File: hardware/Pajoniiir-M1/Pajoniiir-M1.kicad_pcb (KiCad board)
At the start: 4 copper layers, 0 parts

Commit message: feat: establish board-first B8 pre-layout
Populate the live PCB with the complete schematic footprint/net set, preserve fail-closed mechanical gates, and isolate DSI506 as a qualified display profile. Add reproducible placement validation, ERC/BOM evidence, and synchronized project documentation.
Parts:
- added C1: 100nF, Capacitor_SMD:C_0603_1608Metric, F.Cu at (41.9, 93.6)
- added C101: 100nF, Capacitor_SMD:C_0603_1608Metric, F.Cu at (43.6, 232.4)
- added C102: 1uF, Capacitor_SMD:C_0603_1608Metric, F.Cu at (60.6, 232.4)
- added C103: 470pF >=25V, Capacitor_SMD:C_0402_1005Metric, F.Cu at (54.1, 208.7)
- added C104: 100nF, Capacitor_SMD:C_0603_1608Metric, F.Cu at (49.6, 232.4)
- added C105: 10uF, Capacitor_SMD:C_0805_2012Metric, F.Cu at (55.3, 232.7)
- added C106: 22uF DNP, Capacitor_SMD:C_1206_3216Metric, F.Cu at (24.9, 232.8)
- added C107: DNP SI TUNE, Capacitor_SMD:C_0402_1005Metric, F.Cu at (34.9, 232.1)
- added C108: DNP EMI TUNE, Capacitor_SMD:C_0402_1005Metric, F.Cu at (111.3, 241.7)
- added C109: DNP EMI TUNE, Capacitor_SMD:C_0402_1005Metric, F.Cu at (123.6, 241.7)
- added C110: 100nF, Capacitor_SMD:C_0603_1608Metric, F.Cu at (48.0, 93.6)
- added C111: 100nF, Capacitor_SMD:C_0603_1608Metric, F.Cu at (54.1, 93.6)
- added C112: 1uF, Capacitor_SMD:C_0603_1608Metric, F.Cu at (68.3, 101.1)
- added C2: 10uF, Capacitor_SMD:C_0805_2012Metric, F.Cu at (57.9, 101.4)
- added C20: 10uF >=10V, Capacitor_SMD:C_0805_2012Metric, F.Cu at (59.1, 72.6)
- added C21: 100nF >=10V, Capacitor_SMD:C_0603_1608Metric, F.Cu at (70.7, 72.3)
- added C22: 3.3nF, Capacitor_SMD:C_0603_1608Metric, F.Cu at (41.4, 101.1)
- added C23: 22uF >=6.3V, Capacitor_SMD:C_1206_3216Metric, F.Cu at (69.1, 66.1)
- added C24: 22uF DNP RESERVE, Capacitor_SMD:C_1206_3216Metric, F.Cu at (45.5, 53.8)
- added C25: 100nF, Capacitor_SMD:C_0603_1608Metric, F.Cu at (60.1, 93.6)
- added C26: 100nF, Capacitor_SMD:C_0603_1608Metric, F.Cu at (69.3, 158.9)
- added C27: 10nF, Capacitor_SMD:C_0402_1005Metric, F.Cu at (83.5, 170.7)
- added C28: 100nF, Capacitor_SMD:C_0603_1608Metric, F.Cu at (75.3, 158.9)
- added C29: 4.7uF, Capacitor_SMD:C_0603_1608Metric, F.Cu at (47.5, 170.9)
- added C30: 1uF, Capacitor_SMD:C_0603_1608Metric, F.Cu at (22.6, 177.2)
- added C31: 100nF, Capacitor_SMD:C_0603_1608Metric, F.Cu at (81.4, 158.9)
- added C32: 1uF, Capacitor_SMD:C_0603_1608Metric, F.Cu at (26.9, 177.2)
- added C33: 100nF, Capacitor_SMD:C_0603_1608Metric, F.Cu at (87.5, 158.9)
- added C34: 1uF, Capacitor_SMD:C_0603_1608Metric, F.Cu at (31.3, 177.2)
- added C35: 100nF, Capacitor_SMD:C_0603_1608Metric, F.Cu at (23.4, 165.2)
- added C36: 1uF, Capacitor_SMD:C_0603_1608Metric, F.Cu at (35.6, 177.2)
- added C37: 1uF, Capacitor_SMD:C_0603_1608Metric, F.Cu at (40.0, 177.2)
- added C38: 10nF, Capacitor_SMD:C_0402_1005Metric, F.Cu at (88.6, 170.7)
- added C39: 100nF, Capacitor_SMD:C_0603_1608Metric, F.Cu at (29.5, 165.2)
- added C4: 4.7nF, Capacitor_SMD:C_0603_1608Metric, F.Cu at (47.0, 101.1)
- added C40: 4.7uF, Capacitor_SMD:C_0805_2012Metric, F.Cu at (63.4, 159.2)
- added C41: 22uF, Capacitor_SMD:C_0805_2012Metric, F.Cu at (52.8, 171.2)
- added C42: 22pF C0G, Capacitor_SMD:C_0402_1005Metric, F.Cu at (72.4, 149.7)
- added C43: 10uF, Capacitor_SMD:C_0805_2012Metric, F.Cu at (57.9, 171.2)
- added C44: 100nF, Capacitor_SMD:C_0603_1608Metric, F.Cu at (35.6, 165.2)
- added C45: 100nF, Capacitor_SMD:C_0603_1608Metric, F.Cu at (41.6, 165.2)
- added C46: 100nF, Capacitor_SMD:C_0603_1608Metric, F.Cu at (47.7, 165.2)
- added C47: 100nF, Capacitor_SMD:C_0603_1608Metric, F.Cu at (53.8, 165.2)
- added C48: 10uF, Capacitor_SMD:C_0805_2012Metric, F.Cu at (63.1, 171.2)
- added C49: 100nF, Capacitor_SMD:C_0603_1608Metric, F.Cu at (59.8, 165.2)
- added C5: 4.7nF, Capacitor_SMD:C_0603_1608Metric, F.Cu at (52.6, 101.1)
- added C50: 100nF, Capacitor_SMD:C_0603_1608Metric, F.Cu at (65.9, 165.2)
- added C51: 100nF, Capacitor_SMD:C_0603_1608Metric, F.Cu at (72.0, 165.2)
- added C52: 100nF, Capacitor_SMD:C_0603_1608Metric, F.Cu at (78.1, 165.2)
- added C53: 100nF, Capacitor_SMD:C_0603_1608Metric, F.Cu at (84.1, 165.2)
- added C54: 100nF, Capacitor_SMD:C_0603_1608Metric, F.Cu at (23.4, 170.9)
- added C55: 10uF, Capacitor_SMD:C_0805_2012Metric, F.Cu at (68.2, 171.2)
- added C56: 100nF, Capacitor_SMD:C_0603_1608Metric, F.Cu at (29.5, 170.9)
- added C57: 10uF, Capacitor_SMD:C_0805_2012Metric, F.Cu at (73.3, 171.2)
- added C58: 100nF, Capacitor_SMD:C_0603_1608Metric, F.Cu at (35.6, 170.9)
- added C59: 10uF, Capacitor_SMD:C_0805_2012Metric, F.Cu at (78.4, 171.2)
- added C6: 100nF, Capacitor_SMD:C_0603_1608Metric, F.Cu at (66.2, 93.6)
- added C60: 100nF, Capacitor_SMD:C_0603_1608Metric, F.Cu at (41.6, 170.9)
- added C61: 15pF C0G, Capacitor_SMD:C_0402_1005Metric, F.Cu at (81.2, 149.7)
- added C62: 15pF C0G, Capacitor_SMD:C_0402_1005Metric, F.Cu at (24.8, 158.6)
- added C63: 1uF, Capacitor_SMD:C_0603_1608Metric, F.Cu at (44.4, 177.2)
- added C64: 100nF, Capacitor_SMD:C_0603_1608Metric, F.Cu at (138.6, 165.9)
- added C65: 10uF, Capacitor_SMD:C_0805_2012Metric, F.Cu at (144.2, 166.1)
- added C66: 22uF, Capacitor_SMD:C_1206_3216Metric, F.Cu at (132.7, 166.3)
- added C67: 1uF, Capacitor_SMD:C_0603_1608Metric, F.Cu at (106.6, 172.5)
- added C68: 10uF, Capacitor_SMD:C_0805_2012Metric, F.Cu at (63.1, 101.4)
- added C69: 100nF, Capacitor_SMD:C_0603_1608Metric, F.Cu at (72.3, 93.6)
- added C7: 22uF, Capacitor_SMD:C_1206_3216Metric, F.Cu at (36.0, 94.0)
- added C70: 100nF, Capacitor_SMD:C_0603_1608Metric, F.Cu at (23.4, 101.1)
- added C71: 47uF, Capacitor_SMD:C_1210_3225Metric, F.Cu at (70.4, 87.0)
- added C72: 100uF DNP, Capacitor_SMD:C_1210_3225Metric, F.Cu at (38.7, 73.2)
- added C73: 100nF, Capacitor_SMD:C_0603_1608Metric, F.Cu at (29.5, 101.1)
- added C74: 100nF, Capacitor_SMD:C_0603_1608Metric, F.Cu at (35.6, 101.1)
- added C75: 47uF, Capacitor_SMD:C_1210_3225Metric, F.Cu at (23.3, 94.5)
- added C76: 100uF DNP, Capacitor_SMD:C_1210_3225Metric, F.Cu at (48.6, 73.2)
- added C77: 1nF DNP, Capacitor_SMD:C_0603_1608Metric, F.Cu at (119.0, 69.5)
- added C78: DNP EMI TUNE, Capacitor_SMD:C_0402_1005Metric, F.Cu at (96.6, 69.2)
- added C79: DNP EMI TUNE, Capacitor_SMD:C_0402_1005Metric, F.Cu at (108.9, 69.2)
- added C80: 1nF DNP, Capacitor_SMD:C_0603_1608Metric, F.Cu at (127.0, 69.5)
- added C81: 10uF, Capacitor_SMD:C_0805_2012Metric, F.Cu at (179.4, 60.3)
- added C82: 100nF, Capacitor_SMD:C_0603_1608Metric, F.Cu at (191.0, 44.2)
- added C83: 10uF, Capacitor_SMD:C_0805_2012Metric, F.Cu at (184.5, 60.3)
- added C84: 100nF, Capacitor_SMD:C_0603_1608Metric, F.Cu at (150.4, 60.1)
- added C85: 10uF, Capacitor_SMD:C_0805_2012Metric, F.Cu at (189.6, 60.3)
- added C86: 100nF, Capacitor_SMD:C_0603_1608Metric, F.Cu at (156.5, 60.1)
- added C87: 10uF, Capacitor_SMD:C_0805_2012Metric, F.Cu at (150.0, 66.6)
- added C88: 2.2uF, Capacitor_SMD:C_0603_1608Metric, F.Cu at (168.4, 60.1)
- added C89: 2.2uF, Capacitor_SMD:C_0603_1608Metric, F.Cu at (174.0, 60.1)
- added C90: 100nF, Capacitor_SMD:C_0603_1608Metric, F.Cu at (162.6, 60.1)
- added C91: 2.2nF C0G, Capacitor_SMD:C_0603_1608Metric, F.Cu at (174.0, 44.2)
- added C92: 2.2nF C0G, Capacitor_SMD:C_0603_1608Metric, F.Cu at (183.3, 44.2)
- added C93: 100nF, Capacitor_SMD:C_0603_1608Metric, F.Cu at (179.4, 147.6)
- added C94: 10uF, Capacitor_SMD:C_0805_2012Metric, F.Cu at (185.0, 147.9)
- added D1: SMBJ6.0CA-TR, Diode_SMD:D_SMB, F.Cu at (53.8, 45.9)
- added D2: TPD2EUSB30ADRTR, Package_TO_SOT_SMD:Texas_DRT-3, F.Cu at (115.5, 28.3)
- added D3: TPD2EUSB30ADRTR, Package_TO_SOT_SMD:Texas_DRT-3, F.Cu at (115.5, 48.9)
- added FB1: 0R / FERRITE OPTION, Resistor_SMD:R_0603_1608Metric, F.Cu at (29.4, 60.0)
- added FB2: 0R / FERRITE OPTION, Resistor_SMD:R_0603_1608Metric, F.Cu at (47.4, 60.0)
- added FB3: 0R / ferrite option, Resistor_SMD:R_0603_1608Metric, F.Cu at (168.4, 147.6)
- added J10: C6 DEBUG TC2030-NL DNL, Connector:Tag-Connect_TC2030-IDC-NL_2x03_P1.27mm_Vertical, F.Cu at (91.5, 228.6)
- added J2: 87520-1010ALF, Pajoniiir-M1:Amphenol_87520-1010ALF, F.Cu at (95.6, 30.0)
- added J3: 87520-1010ALF, Pajoniiir-M1:Amphenol_87520-1010ALF, F.Cu at (95.6, 50.6)
- added J4: KLPX-0848A-2-W-G, Pajoniiir-M1:Kycon_KLPX-0848A-2-x-G, F.Cu at (174.5, 33.3)
- added J5: KLPX-0848A-2-R-G, Pajoniiir-M1:Kycon_KLPX-0848A-2-x-G, F.Cu at (162.1, 49.2)
- added J6: 15-pin Raspberry-Pi-style DSI host, Pajoniiir-M1:Amphenol_SFW15R-2STE1LF, F.Cu at (175.2, 137.5)
- added J7: 503398-1892, Pajoniiir-M1:Molex_503398-1892, F.Cu at (27.8, 217.8)
- added J8: P4 DEBUG TC2030-NL DNL, Connector:Tag-Connect_TC2030-IDC-NL_2x03_P1.27mm_Vertical, F.Cu at (91.5, 209.8)
- added J9: P4 USB SERIAL/JTAG FACTORY POGO DNL, Pajoniiir-M1:Factory_Pogo_USBJTAG_1x05_P1.27_2Tooling, F.Cu at (96.9, 219.4)
- added L1: XGL4030-222MEC / 2.2uH, Inductor_SMD:L_Coilcraft_XxL4030, F.Cu at (31.4, 151.6)
- added L2: XGL4030-222MEC / 2.2uH, Inductor_SMD:L_Coilcraft_XxL4030, F.Cu at (59.0, 29.8)
- added R1: 402k 1%, Resistor_SMD:R_0603_1608Metric, F.Cu at (32.6, 86.1)
- added R100: 4.7k DNP, Resistor_SMD:R_0603_1608Metric, F.Cu at (174.5, 160.2)
- added R104: 100k, Resistor_SMD:R_0603_1608Metric, F.Cu at (23.1, 239.0)
- added R105: 100R, Resistor_SMD:R_0603_1608Metric, F.Cu at (28.4, 239.0)
- added R106: 0R, Resistor_SMD:R_0402_1005Metric, F.Cu at (23.1, 244.5)
- added R107: 0R, Resistor_SMD:R_0402_1005Metric, F.Cu at (28.4, 244.5)
- added R108: 0R, Resistor_SMD:R_0402_1005Metric, F.Cu at (33.7, 244.5)
- added R109: 22R, Resistor_SMD:R_0402_1005Metric, F.Cu at (39.0, 244.5)
- added R110: 0R, Resistor_SMD:R_0402_1005Metric, F.Cu at (44.3, 244.5)
- added R111: 0R, Resistor_SMD:R_0402_1005Metric, F.Cu at (49.6, 244.5)
- added R112: 10k, Resistor_SMD:R_0603_1608Metric, F.Cu at (33.7, 239.0)
- added R113: 10k, Resistor_SMD:R_0603_1608Metric, F.Cu at (39.0, 239.0)
- added R114: 10k, Resistor_SMD:R_0603_1608Metric, F.Cu at (44.3, 239.0)
- added R115: 10k, Resistor_SMD:R_0603_1608Metric, F.Cu at (49.6, 239.0)
- added R116: 10k, Resistor_SMD:R_0603_1608Metric, F.Cu at (54.9, 239.0)
- added R117: 10k, Resistor_SMD:R_0603_1608Metric, F.Cu at (60.2, 239.0)
- added R118: 22R, Resistor_SMD:R_0402_1005Metric, F.Cu at (97.0, 248.0)
- added R119: 22R, Resistor_SMD:R_0402_1005Metric, F.Cu at (102.3, 248.0)
- added R120: WSK25125L000FEA / 5mR 1% 1W, Resistor_SMD:R_Shunt_Vishay_WSK2512_6332Metric_T1.19mm, F.Cu at (34.0, 45.6)
- added R121: 10R, Resistor_SMD:R_0603_1608Metric, F.Cu at (73.6, 101.1)
- added R122: 10R, Resistor_SMD:R_0603_1608Metric, F.Cu at (23.1, 107.4)
- added R123: 10k, Resistor_SMD:R_0603_1608Metric, F.Cu at (28.4, 107.4)
- added R2: 150k 1%, Resistor_SMD:R_0603_1608Metric, F.Cu at (40.5, 86.1)
- added R20: 100k, Resistor_SMD:R_0603_1608Metric, F.Cu at (33.6, 107.4)
- added R21: 100k PG PULLUP, Resistor_SMD:R_0603_1608Metric, F.Cu at (43.7, 65.7)
- added R22: 0R FSW LOW, Resistor_SMD:R_0603_1608Metric, F.Cu at (25.8, 79.8)
- added R23: 0R DEF LOW, Resistor_SMD:R_0603_1608Metric, F.Cu at (36.6, 79.8)
- added R24: 4.02k 1%, Resistor_SMD:R_0402_1005Metric, F.Cu at (33.5, 158.6)
- added R25: 0R, Resistor_SMD:R_0603_1608Metric, F.Cu at (48.7, 177.2)
- added R26: 0R, Resistor_SMD:R_0603_1608Metric, F.Cu at (53.1, 177.2)
- added R27: 499k 1%, Resistor_SMD:R_0402_1005Metric, F.Cu at (41.7, 158.6)
- added R28: 499k 1%, Resistor_SMD:R_0402_1005Metric, F.Cu at (49.6, 158.6)
- added R29: 0R, Resistor_SMD:R_0402_1005Metric, F.Cu at (79.2, 176.9)
- added R3: 562k 1%, Resistor_SMD:R_0603_1608Metric, F.Cu at (48.5, 86.1)
- added R30: 0R, Resistor_SMD:R_0402_1005Metric, F.Cu at (83.5, 176.9)
- added R31: 0R, Resistor_SMD:R_0402_1005Metric, F.Cu at (87.9, 176.9)
- added R32: 0R, Resistor_SMD:R_0402_1005Metric, F.Cu at (22.6, 182.7)
- added R33: 0R, Resistor_SMD:R_0402_1005Metric, F.Cu at (26.9, 182.7)
- added R34: 0R, Resistor_SMD:R_0402_1005Metric, F.Cu at (31.3, 182.7)
- added R35: 10k 1%, Resistor_SMD:R_0603_1608Metric, F.Cu at (57.1, 158.9)
- added R36: 0R, Resistor_SMD:R_0402_1005Metric, F.Cu at (35.6, 182.7)
- added R37: 10k, Resistor_SMD:R_0603_1608Metric, F.Cu at (57.4, 177.2)
- added R38: 10k, Resistor_SMD:R_0603_1608Metric, F.Cu at (61.8, 177.2)
- added R39: 10k, Resistor_SMD:R_0603_1608Metric, F.Cu at (66.1, 177.2)
- added R4: 150k 1%, Resistor_SMD:R_0603_1608Metric, F.Cu at (56.5, 86.1)
- added R40: 33R, Resistor_SMD:R_0603_1608Metric, F.Cu at (70.5, 177.2)
- added R41: 33R, Resistor_SMD:R_0603_1608Metric, F.Cu at (74.8, 177.2)
- added R42: 0R, Resistor_SMD:R_0603_1608Metric, F.Cu at (110.9, 172.5)
- added R43: 10k, Resistor_SMD:R_0603_1608Metric, F.Cu at (115.3, 172.5)
- added R44: 0R, Resistor_SMD:R_0402_1005Metric, F.Cu at (137.1, 172.2)
- added R45: 51.1k 1%, Resistor_SMD:R_0603_1608Metric, F.Cu at (130.1, 133.9)
- added R46: 22R, Resistor_SMD:R_0402_1005Metric, F.Cu at (141.4, 172.2)
- added R47: 0R, Resistor_SMD:R_0402_1005Metric, F.Cu at (106.6, 178.0)
- added R48: 51.1k 1%, Resistor_SMD:R_0603_1608Metric, F.Cu at (138.5, 133.9)
- added R49: 0R, Resistor_SMD:R_0402_1005Metric, F.Cu at (110.9, 178.0)
- added R5: 750R 1%, Resistor_SMD:R_0603_1608Metric, F.Cu at (24.5, 86.1)
- added R50: 51.1k 1%, Resistor_SMD:R_0603_1608Metric, F.Cu at (108.6, 165.9)
- added R51: 0R, Resistor_SMD:R_0402_1005Metric, F.Cu at (115.3, 178.0)
- added R52: 51.1k 1%, Resistor_SMD:R_0603_1608Metric, F.Cu at (117.1, 165.9)
- added R53: 0R, Resistor_SMD:R_0402_1005Metric, F.Cu at (119.6, 178.0)
- added R54: 51.1k 1%, Resistor_SMD:R_0603_1608Metric, F.Cu at (125.5, 165.9)
- added R55: 33R, Resistor_SMD:R_0603_1608Metric, F.Cu at (119.6, 172.5)
- added R56: 33R, Resistor_SMD:R_0603_1608Metric, F.Cu at (124.0, 172.5)
- added R57: 10k, Resistor_SMD:R_0603_1608Metric, F.Cu at (128.4, 172.5)
- added R58: 10k, Resistor_SMD:R_0603_1608Metric, F.Cu at (132.7, 172.5)
- added R59: 100k, Resistor_SMD:R_0603_1608Metric, F.Cu at (38.7, 107.4)
- added R6: 10k PG PULLUP, Resistor_SMD:R_0603_1608Metric, F.Cu at (27.1, 72.3)
- added R60: 10k, Resistor_SMD:R_0603_1608Metric, F.Cu at (48.5, 107.4)
- added R61: 54.9k 1%, Resistor_SMD:R_0603_1608Metric, F.Cu at (62.8, 79.8)
- added R62: 0R / SHUNT OPTION, Resistor_SMD:R_1206_3216Metric, F.Cu at (68.6, 44.8)
- added R63: 100k, Resistor_SMD:R_0603_1608Metric, F.Cu at (43.8, 107.4)
- added R64: 10k, Resistor_SMD:R_0603_1608Metric, F.Cu at (52.9, 107.4)
- added R65: 34.8k 1%, Resistor_SMD:R_0603_1608Metric, F.Cu at (71.3, 79.8)
- added R66: 0R / SHUNT OPTION, Resistor_SMD:R_1206_3216Metric, F.Cu at (28.9, 53.8)
- added R67: 0R, Resistor_SMD:R_0402_1005Metric, F.Cu at (116.0, 75.0)
- added R68: 0R, Resistor_SMD:R_0402_1005Metric, F.Cu at (120.4, 75.0)
- added R69: 0R, Resistor_SMD:R_0603_1608Metric, F.Cu at (107.3, 75.2)
- added R7: 100k 1% PGTH TOP, Resistor_SMD:R_0603_1608Metric, F.Cu at (28.5, 65.7)
- added R70: 1M DNP, Resistor_SMD:R_0603_1608Metric, F.Cu at (94.1, 75.2)
- added R71: 22R, Resistor_SMD:R_0402_1005Metric, F.Cu at (124.7, 75.0)
- added R72: 22R, Resistor_SMD:R_0402_1005Metric, F.Cu at (129.1, 75.0)
- added R73: 0R, Resistor_SMD:R_0603_1608Metric, F.Cu at (111.6, 75.2)
- added R74: 1M DNP, Resistor_SMD:R_0603_1608Metric, F.Cu at (101.4, 75.2)
- added R75: 22R, Resistor_SMD:R_0402_1005Metric, F.Cu at (175.7, 66.1)
- added R76: 22R, Resistor_SMD:R_0402_1005Metric, F.Cu at (180.1, 66.1)
- added R77: 22R, Resistor_SMD:R_0402_1005Metric, F.Cu at (184.4, 66.1)
- added R78: 100R, Resistor_SMD:R_0603_1608Metric, F.Cu at (155.2, 66.3)
- added R79: 100k, Resistor_SMD:R_0603_1608Metric, F.Cu at (171.0, 66.3)
- added R8: 36.5k 1% PGTH BOT, Resistor_SMD:R_0603_1608Metric, F.Cu at (64.7, 60.0)
- added R80: 470R, Resistor_SMD:R_0603_1608Metric, F.Cu at (160.5, 66.3)
- added R81: 470R, Resistor_SMD:R_0603_1608Metric, F.Cu at (165.8, 66.3)
- added R82: 0R, Resistor_SMD:R_0201_0603Metric, F.Cu at (166.9, 166.1)
- added R83: 0R, Resistor_SMD:R_0201_0603Metric, F.Cu at (171.3, 166.1)
- added R84: 0R, Resistor_SMD:R_0201_0603Metric, F.Cu at (175.6, 166.1)
- added R85: 0R, Resistor_SMD:R_0201_0603Metric, F.Cu at (180.0, 166.1)
- added R86: 0R, Resistor_SMD:R_0201_0603Metric, F.Cu at (184.4, 166.1)
- added R87: 0R, Resistor_SMD:R_0201_0603Metric, F.Cu at (188.7, 166.1)
- added R95: 22R, Resistor_SMD:R_0402_1005Metric, F.Cu at (198.6, 159.9)
- added R96: 22R, Resistor_SMD:R_0402_1005Metric, F.Cu at (162.6, 166.2)
- added R97: 4.7k, Resistor_SMD:R_0603_1608Metric, F.Cu at (189.5, 160.2)
- added R98: 4.7k, Resistor_SMD:R_0603_1608Metric, F.Cu at (194.1, 160.2)
- added R99: 4.7k DNP, Resistor_SMD:R_0603_1608Metric, F.Cu at (183.0, 160.2)
- added SW1: B3U-3000P-B, Button_Switch_SMD:SW_SPST_B3U-3000P-B, F.Cu at (48.8, 151.7)
- added SW2: B3U-3000P-B, Button_Switch_SMD:SW_SPST_B3U-3000P-B, F.Cu at (61.6, 151.7)
- added TP1: 3V3_DISPLAY_MODULE, TestPoint:TestPoint_Pad_D1.5mm, F.Cu at (169.2, 154.1)
- added TP10: J6_I2C_SCL, TestPoint:TestPoint_Pad_D1.5mm, F.Cu at (165.3, 160.4)
- added TP13: BOOT_GPIO36, TestPoint:TestPoint_Pad_D1.5mm, F.Cu at (99.4, 242.2)
- added TP14: C6_BOOT_GPIO8, TestPoint:TestPoint_Pad_D1.5mm, F.Cu at (87.0, 242.2)
- added TP15: DEBUG_UART_TX, TestPoint:TestPoint_Pad_D1.5mm, F.Cu at (118.0, 235.9)
- added TP16: DEBUG_UART_RX, TestPoint:TestPoint_Pad_D1.5mm, F.Cu at (104.6, 235.9)
- added TP17: CHIP_PU, TestPoint:TestPoint_Pad_D1.5mm, F.Cu at (84.3, 248.5)
- added TP18: USBJTAG_DM_SERVICE, TestPoint:TestPoint_Pad_D1.5mm, F.Cu at (111.4, 228.0)
- added TP19: USBJTAG_DP_SERVICE, TestPoint:TestPoint_Pad_D1.5mm, F.Cu at (89.1, 235.9)
- added TP2: P4_LDO_MIPI_2V5, TestPoint:TestPoint_Pad_D1.5mm, F.Cu at (185.2, 154.1)
- added TP20: C6_EN, TestPoint:TestPoint_Pad_D1.5mm, F.Cu at (91.2, 248.5)
- added TP21: 5V_PROTECTED, TestPoint:TestPoint_Pad_D1.5mm, F.Cu at (57.1, 65.9)
- added TP22: 5V_SYS, TestPoint:TestPoint_Pad_D1.5mm, F.Cu at (29.6, 93.8)
- added TP23: 3V3_SYS, TestPoint:TestPoint_Pad_D1.5mm, F.Cu at (54.7, 80.0)
- added TP24: SYS_POWER_ALERT_N, TestPoint:TestPoint_Pad_D1.5mm, F.Cu at (62.1, 53.6)
- added TP25: EFUSE_PG, TestPoint:TestPoint_Pad_D1.5mm, F.Cu at (46.4, 80.0)
- added TP26: 3V3_PG, TestPoint:TestPoint_Pad_D1.5mm, F.Cu at (63.9, 86.3)
- added TP9: J6_I2C_SDA, TestPoint:TestPoint_Pad_D1.5mm, F.Cu at (197.4, 154.1)
- added U1: ESP32-P4NRW32X, Pajoniiir-M1:ESP32-P4, F.Cu at (28.1, 139.1)
- added U12: TPS25221DRVR, Package_SON:WSON-6-1EP_2x2mm_P0.65mm_EP1x1.6mm, F.Cu at (39.6, 37.7)
- added U13: TPS22918DBVR, Package_TO_SOT_SMD:SOT-23-6, F.Cu at (41.7, 209.9)
- added U14: INA238AIDGSR, Pajoniiir-M1:Texas_DGS0010A_VSSOP-10_3x3mm_P0.5mm, F.Cu at (52.0, 37.8)
- added U2: W25Q128JVPIQ, Package_SON:WSON-8-1EP_6x5mm_P1.27mm_EP3.4x4.3mm, F.Cu at (42.1, 135.9)
- added U3: TLV62569DRLR, Package_TO_SOT_SMD:SOT-563, F.Cu at (54.6, 134.1)
- added U4: ESP32-C6-WROOM-1-N4, Pajoniiir-M1:ESP32-C6-WROOM-1, F.Cu at (115.1, 149.5)
- added U5: PCM5102APWR, Package_SO:TSSOP-20_4.4x6.5mm_P0.65mm, F.Cu at (153.6, 31.0)
- added U6: TPS25221DRVR, Package_SON:WSON-6-1EP_2x2mm_P0.65mm_EP1x1.6mm, F.Cu at (26.8, 37.7)
- added U7: TPS259474ARPWR, Pajoniiir-M1:Texas_RPW0010A_VQFN-HR-10_2x2mm, F.Cu at (27.8, 28.9)
- added U8: TPS62132RGTR, Package_DFN_QFN:VQFN-16-1EP_3x3mm_P0.5mm_EP1.68x1.68mm_ThermalVias, F.Cu at (41.6, 29.7)
- added Y1: ECS-400-10-37B2-CKY-TR, Crystal:Crystal_SMD_2016-4Pin_2.0x1.6mm, F.Cu at (72.7, 134.5)
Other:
- board text added: "AUDIO - B8 WORKING GROUP"
- board text added: "C6_RF - B8 WORKING GROUP"
- board text added: "DSI_HOST - B8 WORKING GROUP"
- board text added: "P4_CORE - B8 WORKING GROUP"
- board text added: "POWER_SPINE - B8 WORKING GROUP"
- board text added: "SERVICE - B8 WORKING GROUP"
- board text added: "STORAGE - B8 WORKING GROUP"
- board text added: "USB_EDGES - B8 WORKING GROUP"

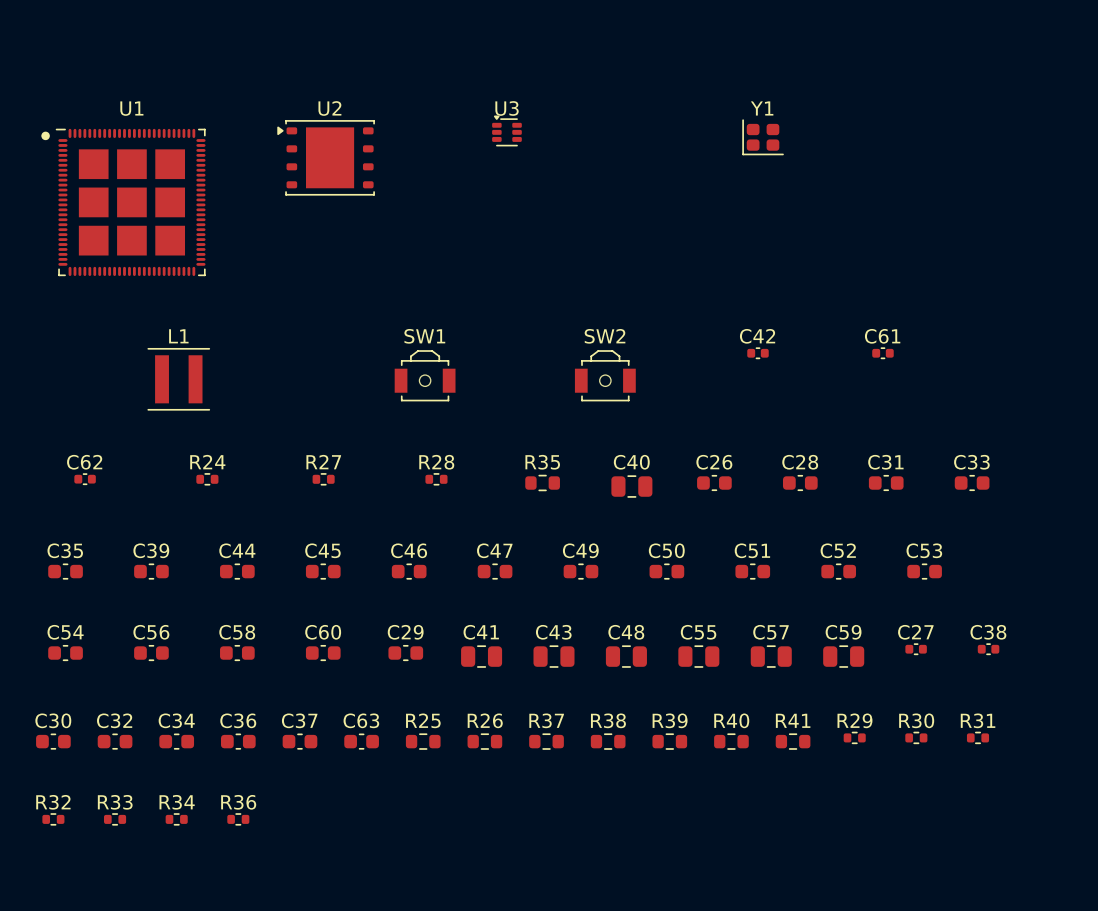
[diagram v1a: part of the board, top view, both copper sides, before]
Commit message: pcb: add B9 P4 core island
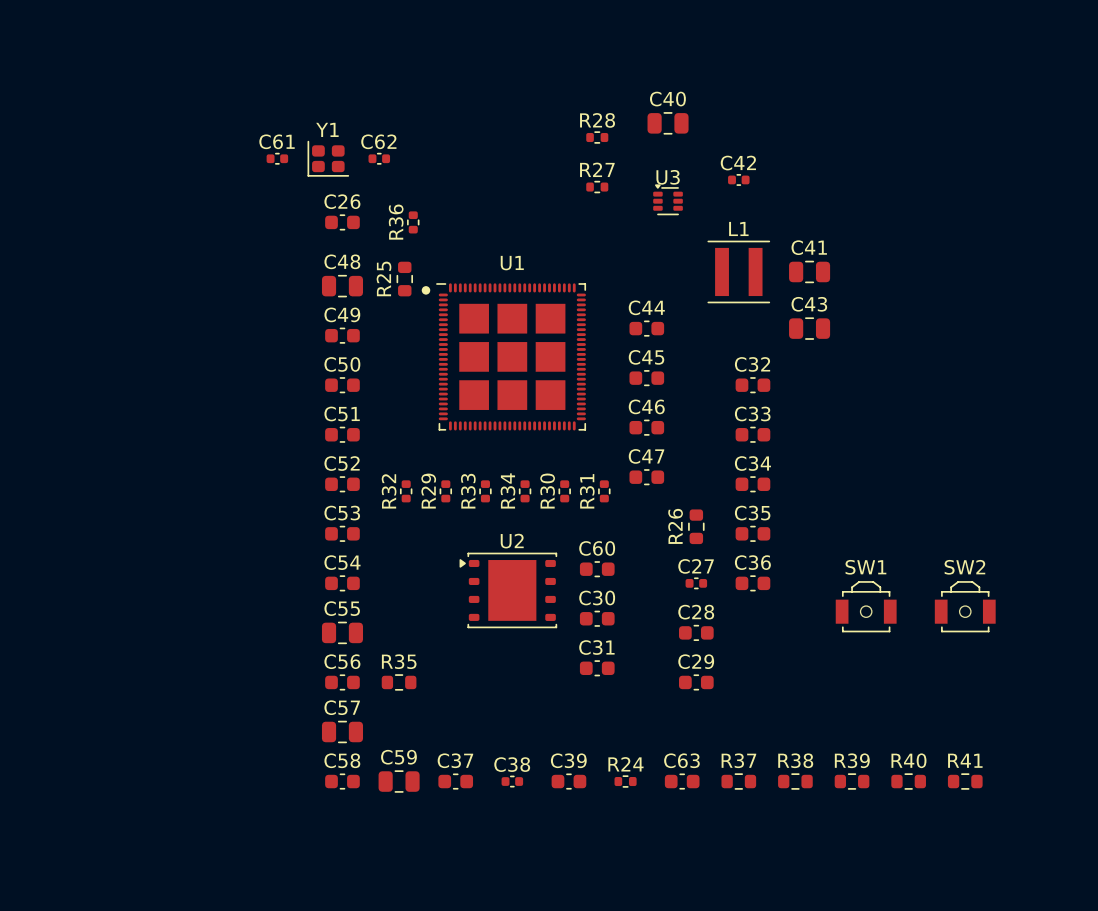
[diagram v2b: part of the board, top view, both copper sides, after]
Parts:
- moved C32 51.6 mm to (72.0, 152.0)
- moved C35 48.6 mm to (72.0, 162.5)
- moved C61 44.9 mm to (38.4, 136.0)
- moved C34 44.6 mm to (72.0, 159.0)
- moved R36 43.9 mm to (48.0, 140.5), turned to 90 degrees
- moved C53 41.2 mm to (43.0, 162.5)
- moved L1 40.3 mm to (71.0, 144.0)
- moved C30 39.4 mm to (61.0, 168.5)
- moved C36 38.0 mm to (72.0, 166.0)
- moved R24 36.5 mm to (63.0, 180.0)
- moved C41 35.7 mm to (76.0, 144.0)
- moved C52 35.6 mm to (43.0, 159.0)
- moved SW1 35.2 mm to (80.0, 168.0)
- moved R33 35.0 mm to (53.1, 159.5), turned to 90 degrees
- moved C38 34.9 mm to (55.0, 180.0)
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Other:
- board text added: "P4_CORE - B9 ROUTING-FEASIBILITY ISLAND"
- board text removed: "P4_CORE - B8 WORKING GROUP"

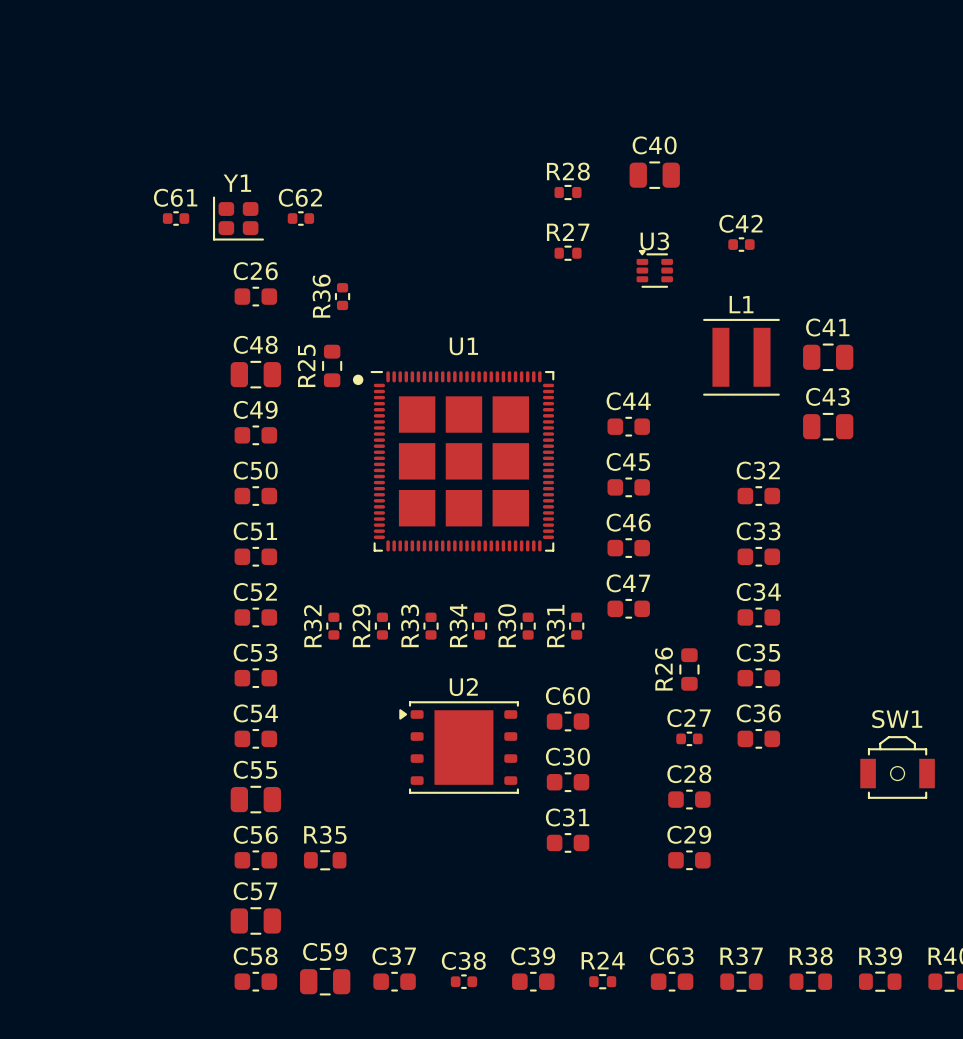
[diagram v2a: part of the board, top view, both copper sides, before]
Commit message: pcb: prove B10 P4 critical routes
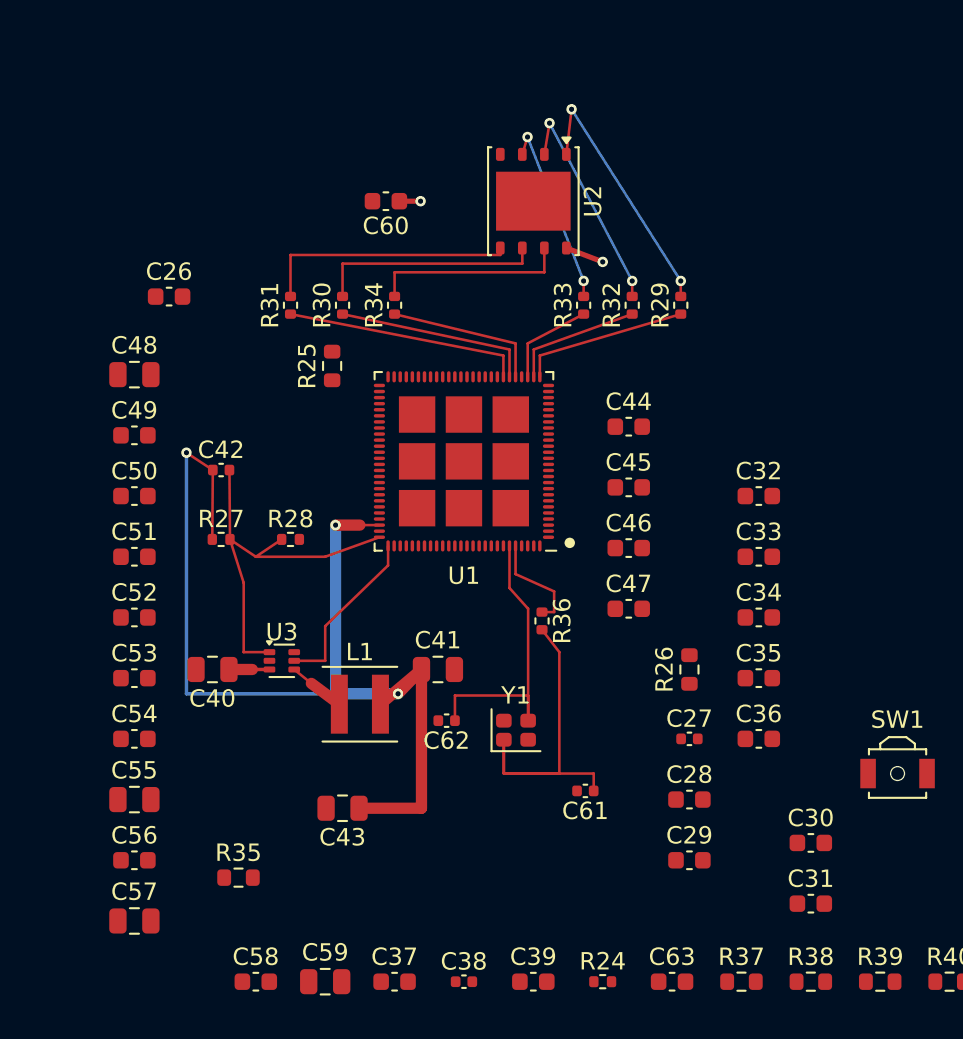
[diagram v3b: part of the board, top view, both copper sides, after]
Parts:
- moved C61 40.6 mm to (62.0, 169.0), turned to 180 degrees
- moved C40 38.2 mm to (40.5, 162.0), turned to 180 degrees
- moved C43 35.6 mm to (48.0, 170.0), turned to 180 degrees
- moved Y1 33.6 mm to (58.0, 165.5)
- moved C42 32.7 mm to (41.0, 150.5)
- moved C60 31.8 mm to (50.5, 135.0), turned to 180 degrees
- moved U2 31.8 mm to (59.0, 135.0), turned to -90 degrees
- moved U3 31.1 mm to (44.5, 161.5)
- moved C62 30.1 mm to (54.0, 164.9), turned to 180 degrees
- moved L1 29.7 mm to (49.0, 164.0)
- moved C41 28.8 mm to (53.5, 162.0)
- moved R27 25.9 mm to (41.0, 154.5)
- moved R28 25.6 mm to (45.0, 154.5)
- moved R29 25.3 mm to (67.5, 141.0)
- moved R32 25.3 mm to (64.7, 141.0)
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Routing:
- net /03_P4_CORE/P4_VDD_HP: track 0.00 -> 64.4 mm, vias 0 -> 3
- net /03_P4_CORE/P4_FB_DCDC: track 0.00 -> 23.0 mm
- net /04_P4_FLASH_CLOCK_RESET/XTAL_P_NODE: track 0.00 -> 21.9 mm
- net /XTAL_N: track 0.00 -> 17.6 mm
- net Net-(U2-~{CS}): track 0.00 -> 15.2 mm, vias 0 -> 2
- net Net-(U2-DI/IO_{0}): track 0.00 -> 14.9 mm
- net /03_P4_CORE/FLASH_VCC: track 0.00 -> 14.5 mm, vias 0 -> 2
- net /03_P4_CORE/FLASH_D: track 0.00 -> 13.7 mm
- net Net-(U2-CLK): track 0.00 -> 13.2 mm
- net Net-(U2-DO/IO_{1}): track 0.00 -> 13.0 mm, vias 0 -> 2
- net Net-(U2-~{HOLD}/~{RESET}/IO_{3}): track 0.00 -> 11.4 mm
- net /03_P4_CORE/FLASH_CK: track 0.00 -> 11.4 mm
- net Net-(U2-~{WP}/IO_{2}): track 0.00 -> 10.8 mm, vias 0 -> 2
- net /03_P4_CORE/P4_EN_DCDC: track 0.00 -> 9.95 mm
- net /04_P4_FLASH_CLOCK_RESET/FLASH_CS: track 0.00 -> 9.69 mm
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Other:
- board text added: "P4_CORE - B10 CRITICAL-ROUTE PROOF"
- board text removed: "P4_CORE - B9 ROUTING-FEASIBILITY ISLAND"

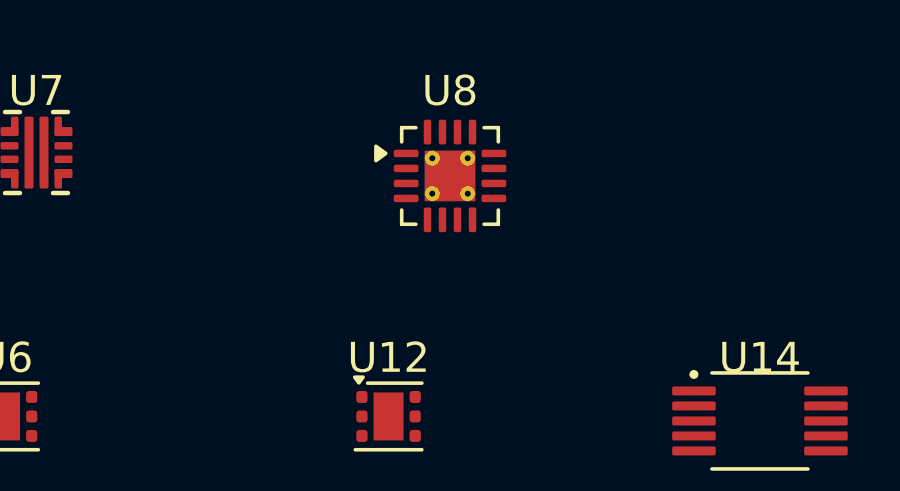
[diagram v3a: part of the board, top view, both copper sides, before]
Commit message: pcb: fix U8 thermal via drill rule
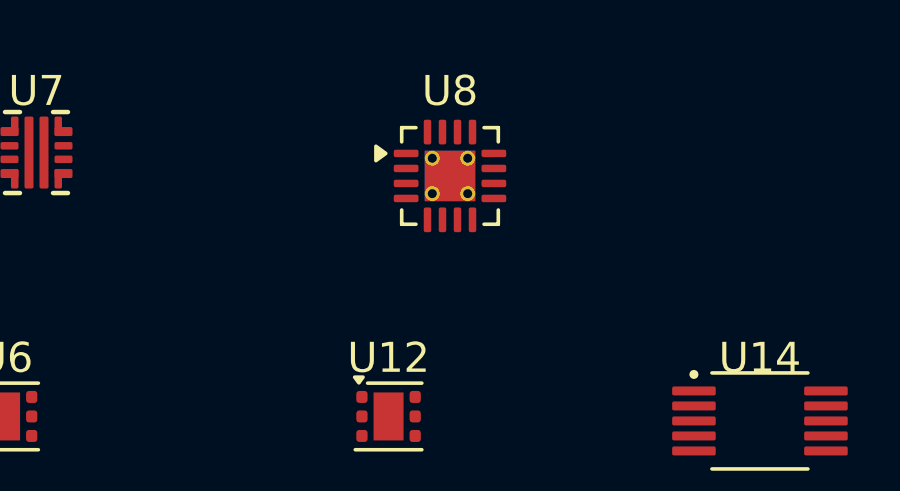
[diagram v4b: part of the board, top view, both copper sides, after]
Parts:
- U8: footprint Package_DFN_QFN:VQFN-16-1EP_3x3mm_P0.5mm_EP1.68x1.68mm_ThermalVias -> Pajoniiir-M1:VQFN-16-1EP_3x3mm_P0.5mm_EP1.68x1.68mm_ThermalVias
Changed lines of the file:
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@@
 		)
 	)
-	(footprint "Package_DFN_QFN:VQFN-16-1EP_3x3mm_P0.5mm_EP1.68x1.68mm_ThermalVias"
+	(footprint "Pajoniiir-M1:VQFN-16-1EP_3x3mm_P0.5mm_EP1.68x1.68mm_ThermalVias"
 		(placed yes)
 		(layer "F.Cu")
@@
 			(at -0.59 -0.59)
 			(size 0.5 0.5)
-			(drill 0.2)
+			(drill 0.3)
 			(property pad_prop_heatsink)
 			(layers "*.Cu")
@@
 			(at -0.59 0.59)
 			(size 0.5 0.5)
-			(drill 0.2)
+			(drill 0.3)
 			(property pad_prop_heatsink)
 			(layers "*.Cu")
@@
 			(at 0.59 -0.59)
 			(size 0.5 0.5)
-			(drill 0.2)
+			(drill 0.3)
 			(property pad_prop_heatsink)
 			(layers "*.Cu")
@@
 			(at 0.59 0.59)
 			(size 0.5 0.5)
-			(drill 0.2)
+			(drill 0.3)
 			(property pad_prop_heatsink)
 			(layers "*.Cu")
